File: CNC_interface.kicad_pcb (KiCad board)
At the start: 2 copper layers, 86.4 x 99.1 mm, 35 parts, among them J1 Conn_01x04_Male, J10 Conn_01x08, J11 Conn_01x08, J12 Conn_01x08, J13 Conn_01x08, J14 Conn_01x03_Male, J15 Conn_01x03_Male, J16 Conn_01x03_Male, J17 Conn_01x08, J18 Conn_01x10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

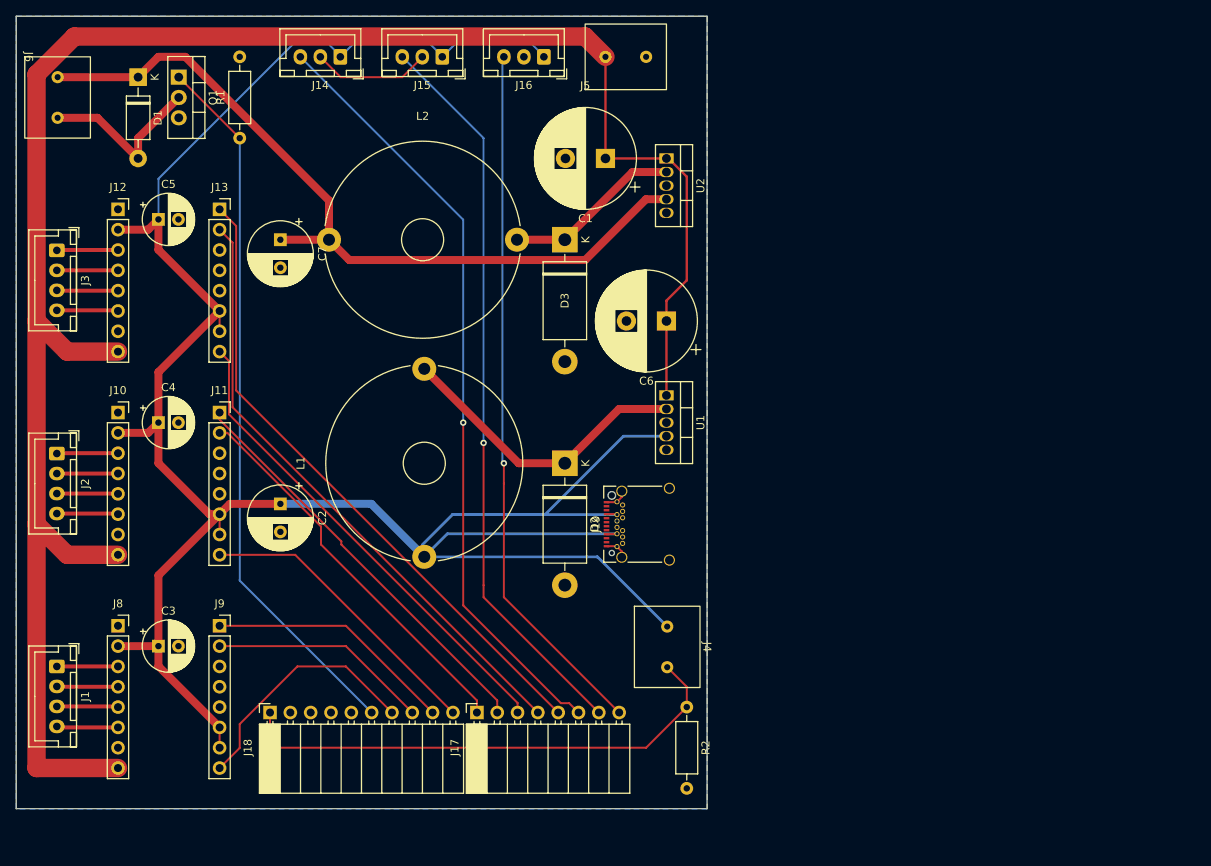
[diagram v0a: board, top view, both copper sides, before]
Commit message: connect step motors to 12V
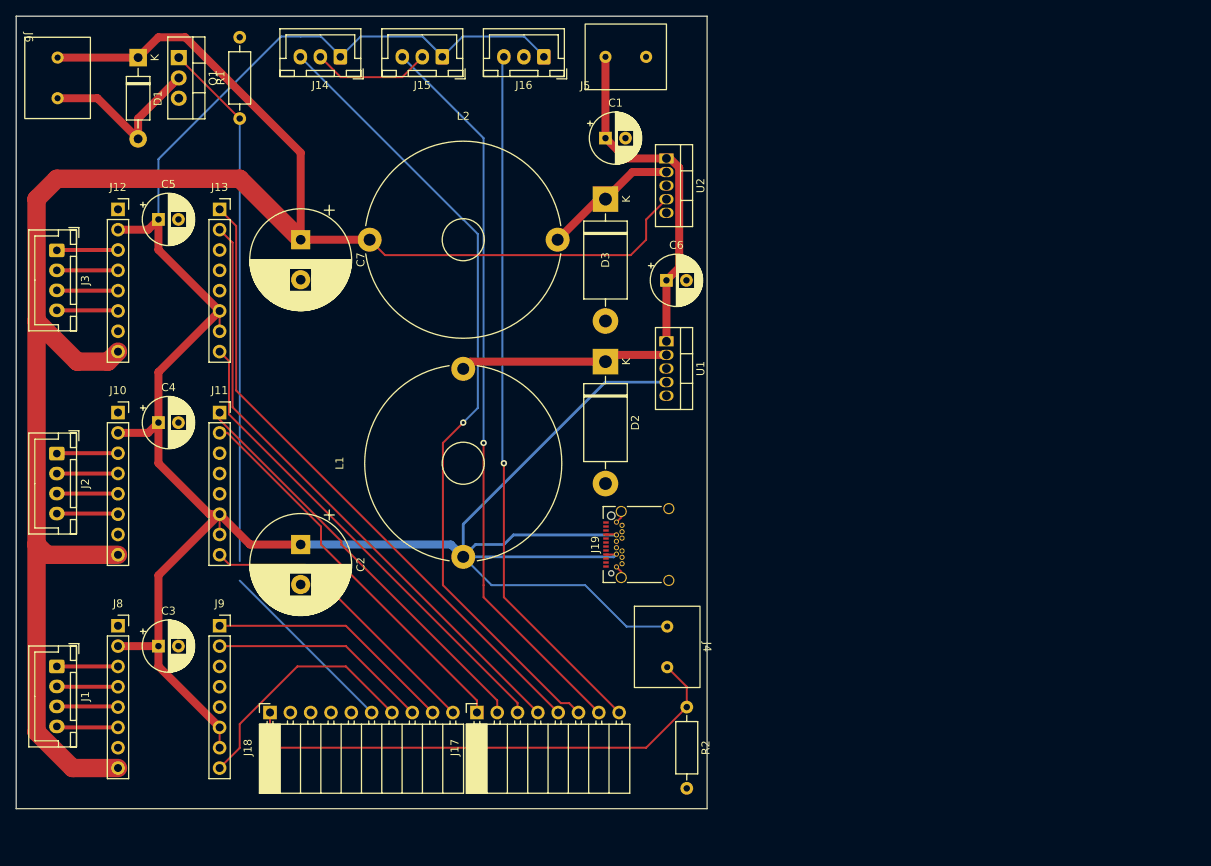
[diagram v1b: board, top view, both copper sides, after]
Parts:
- C1, C6: footprint Capacitor_THT:CP_Radial_D12.5mm_P5.00mm -> Capacitor_THT:CP_Radial_D6.3mm_P2.50mm
- C2, C7: footprint Capacitor_THT:CP_Radial_D8.0mm_P3.50mm -> Capacitor_THT:CP_Radial_D12.5mm_P5.00mm
- moved D2 13.7 mm to (119.4, 73.7)
- moved D3 7.18 mm to (119.4, 53.3)
- moved U1 6.76 mm to (127.0, 71.1)
- moved C2 5.68 mm to (81.3, 96.5)
- moved L2 5.08 mm to (89.9, 58.2)
- moved C6 5.08 mm to (127.0, 63.5), turned to 0 degrees
- moved L1 4.87 mm to (101.4, 98.1)
- moved J19 2.54 mm to (124.5, 96.5)
- moved C7 2.54 mm to (81.3, 58.4)
- moved C1 2.54 mm to (119.4, 45.7), turned to 0 degrees
- moved D1 2.45 mm to (61.0, 35.7)
- moved J6 2.45 mm to (46.8, 33.1)
- moved Q1 2.45 mm to (66.0, 35.7)
- moved R1 2.45 mm to (73.7, 43.3)
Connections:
- J10 pad 8: +24V -> +12V
- J12 pad 8: +24V -> +12V
- J8 pad 8: +24V -> +12V
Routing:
- net +24V: track 246.8 -> 43.5 mm
- net +12V: track 99.8 -> 238.6 mm
- net Net-(D2-Pad1): track 38.0 -> 26.1 mm
- net +5V: track 319.0 -> 312.3 mm
- net Net-(D3-Pad1): track 22.2 -> 17.1 mm
- net Lx: track 97.0 -> 100.6 mm
- net GND: track 20.8 -> 18.1 mm
- removed copper zone on B.Cu, net GND

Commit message: place components
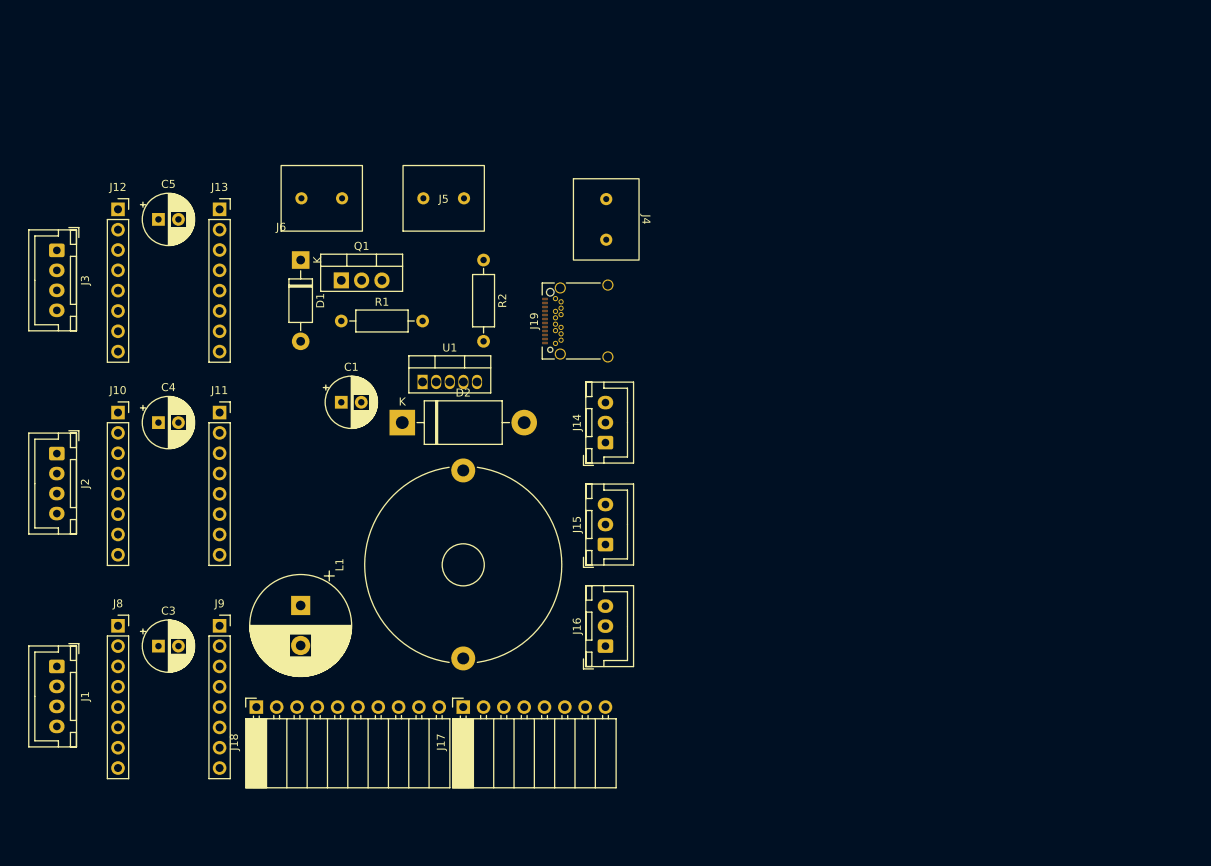
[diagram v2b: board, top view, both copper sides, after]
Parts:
- removed C6: 100µF, Capacitor_THT:CP_Radial_D6.3mm_P2.50mm
- removed C7: 1000µF, Capacitor_THT:CP_Radial_D12.5mm_P5.00mm
- removed D3: 1N5822, Diode_THT:D_DO-201AD_P15.24mm_Horizontal
- removed L2: 220µH, CNC_interface:L_Radial_24.4mm_P23.50mm_Murata_1400series
- removed U2: LM2576HVT-12, Package_TO_SOT_THT:TO-220-5_Vertical
- moved J16 74.1 mm to (119.4, 109.2), turned to 90 degrees
- moved J15 64.3 mm to (119.4, 96.5), turned to 90 degrees
- moved R2 61.4 mm to (104.1, 61.0)
- moved J14 58.5 mm to (119.4, 83.8), turned to 90 degrees
- moved J4 54.0 mm to (115.4, 50.8)
- moved C1 46.7 mm to (86.4, 78.7)
- moved J6 40.2 mm to (78.8, 57.3), turned to 0 degrees
- moved Q1 34.5 mm to (86.4, 63.5), turned to 0 degrees
- moved D1 32.5 mm to (81.3, 61.0)
- moved U1 30.9 mm to (96.5, 76.2), turned to 0 degrees
- moved J19 29.0 mm to (116.8, 68.6)
- moved J5 28.8 mm to (94.1, 57.3)
- moved R1 28.3 mm to (86.4, 68.6), turned to 0 degrees
- moved D2 26.5 mm to (94.0, 81.3), turned to 0 degrees
- moved L1 12.7 mm to (101.4, 110.8)
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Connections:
- C1 pad 1: +24V -> +12V
- J5 pad 1: +24V -> +12V
- U1 pad 1: +24V -> +12V
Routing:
- net +5V: track 312.3 -> 0.00 mm
- net +12V: track 238.6 -> 0.00 mm
- net Lx: track 100.6 -> 0.00 mm, vias 1 -> 0
- net Ly: track 92.1 -> 0.00 mm, vias 1 -> 0
- net DCtrl: track 89.4 -> 0.00 mm
- net Lz: track 88.1 -> 0.00 mm, vias 1 -> 0
- net DIRz: track 80.4 -> 0.00 mm
- net STEPz: track 76.8 -> 0.00 mm
- net CONT: track 63.8 -> 0.00 mm
- net ENz: track 60.5 -> 0.00 mm
- net DIRy: track 51.9 -> 0.00 mm
- net STEPy: track 48.8 -> 0.00 mm
- net +24V: track 43.5 -> 0.00 mm
- net ENy: track 37.3 -> 0.00 mm
- net DIRx: track 31.1 -> 0.00 mm
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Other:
- board outline removed

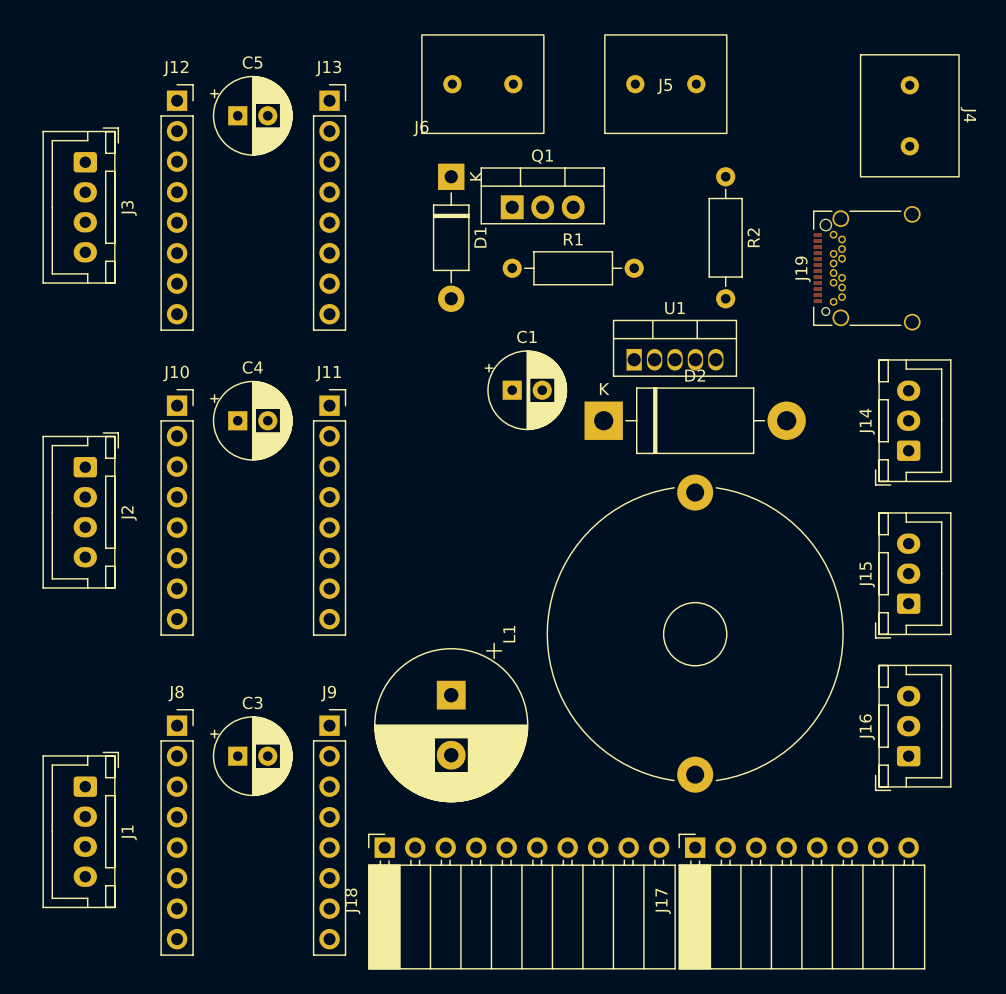
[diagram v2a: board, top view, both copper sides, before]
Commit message: Route PCB + silkscreen
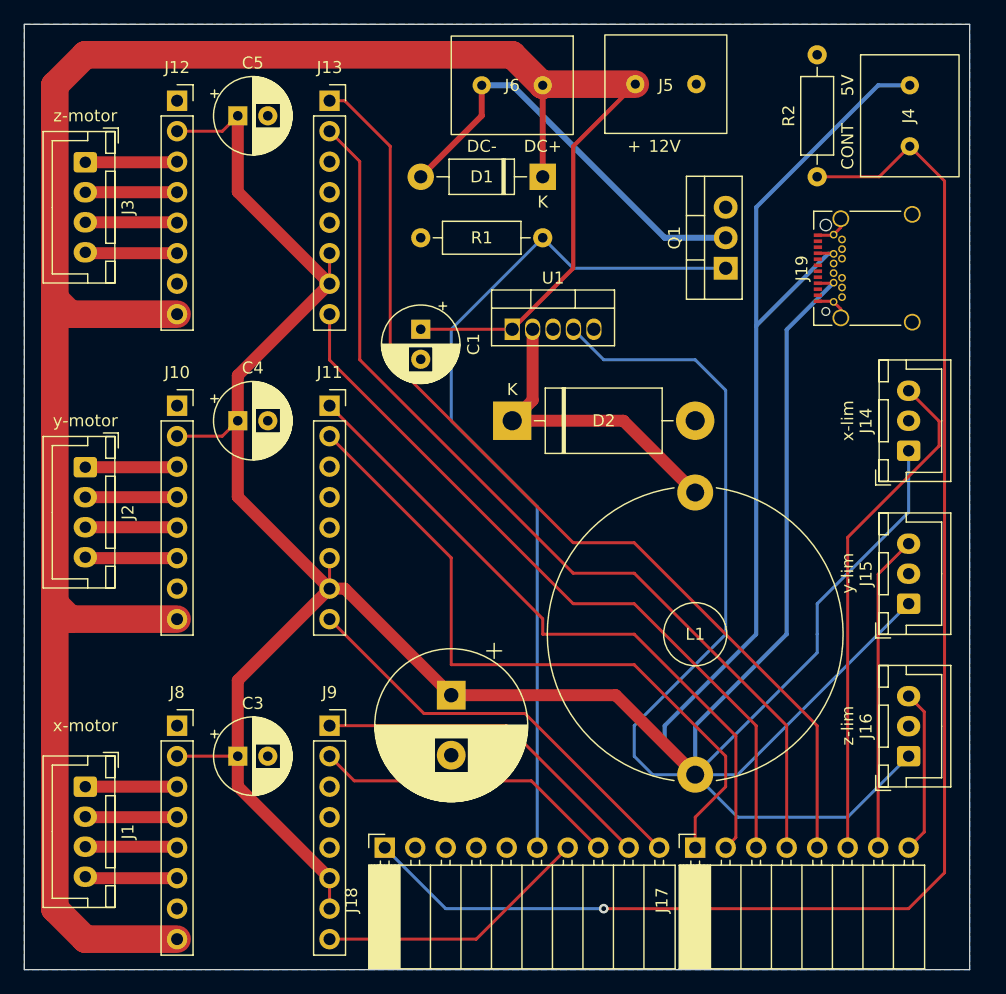
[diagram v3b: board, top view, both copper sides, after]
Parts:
- moved Q1 18.5 mm to (104.1, 68.6), turned to 90 degrees
- moved J6 15.0 mm to (91.4, 49.2), turned to 180 degrees
- moved U1 10.5 mm to (86.4, 73.7)
- moved C1 9.16 mm to (78.7, 73.7), turned to -90 degrees
- moved D1 7.62 mm to (88.9, 61.0), turned to 180 degrees
- moved D2 7.62 mm to (86.4, 81.3)
- moved R2 7.62 mm to (111.8, 61.0), turned to 90 degrees
- moved R1 3.59 mm to (88.9, 66.0), turned to 180 degrees
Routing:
- net +5V: track 0.00 -> 399.7 mm
- net +12V: track 0.00 -> 191.7 mm
- net CONT: track 0.00 -> 120.4 mm, vias 0 -> 1
- net DIRz: track 0.00 -> 82.8 mm
- net STEPz: track 0.00 -> 78.4 mm
- net DCtrl: track 0.00 -> 73.2 mm
- net ENz: track 0.00 -> 62.1 mm
- net STEPy: track 0.00 -> 57.9 mm
- net DIRy: track 0.00 -> 55.6 mm
- net Lx: track 0.00 -> 42.3 mm
- net ENy: track 0.00 -> 35.3 mm
- net DC-: track 0.00 -> 35.3 mm
- net DIRx: track 0.00 -> 29.1 mm
- net Ly: track 0.00 -> 26.4 mm
- net Net-(D2-Pad1): track 0.00 -> 26.0 mm
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- added copper zone on B.Cu, net GND
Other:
- board outline added: 78.7 x 78.7 mm
- board text added: "+"
- board text added: "12V"
- board text added: "5V"
- board text added: "CONT"
- board text added: "DC+"
- board text added: "DC-"
- board text added: "x-lim"
- board text added: "x-motor"
- board text added: "y-lim"
- board text added: "y-motor"
- board text added: "z-lim"
- board text added: "z-motor"

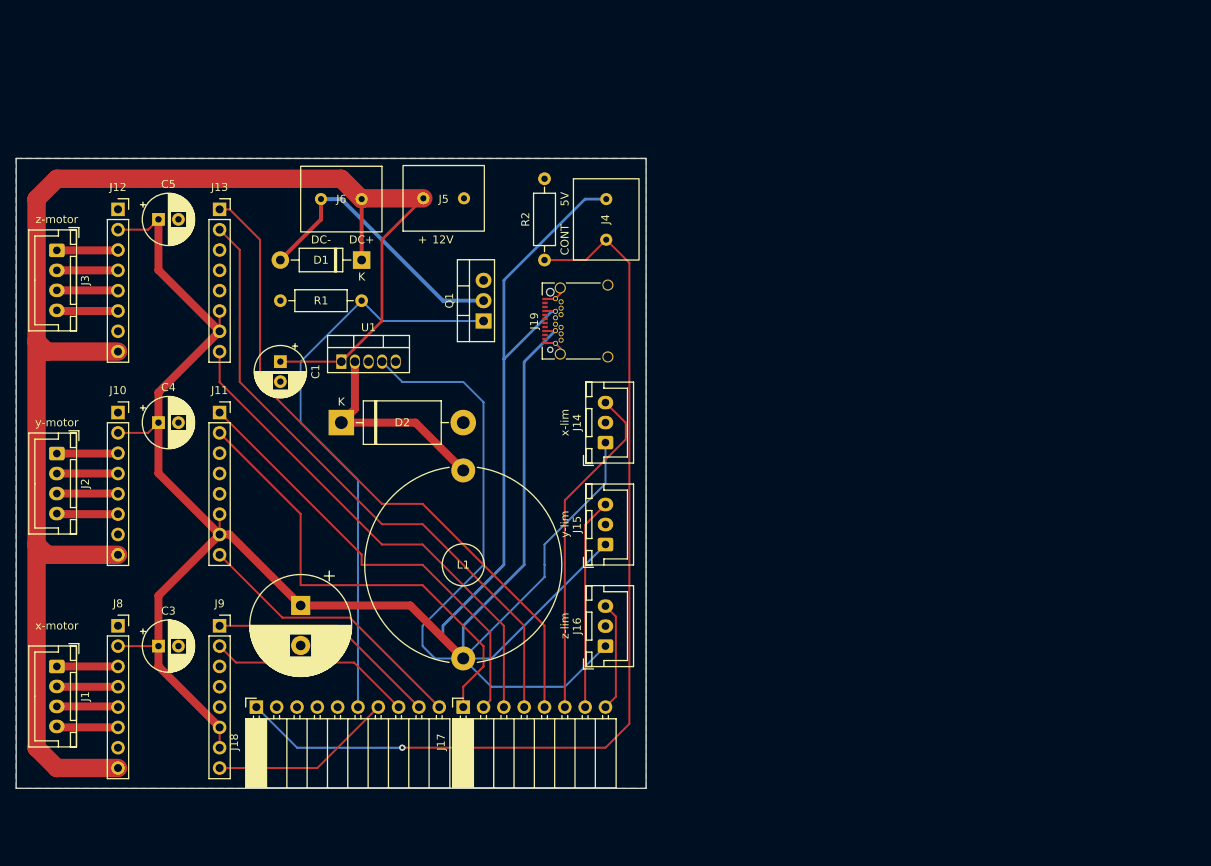
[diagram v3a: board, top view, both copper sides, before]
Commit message: Finish pcb silkscreen and mounting pins
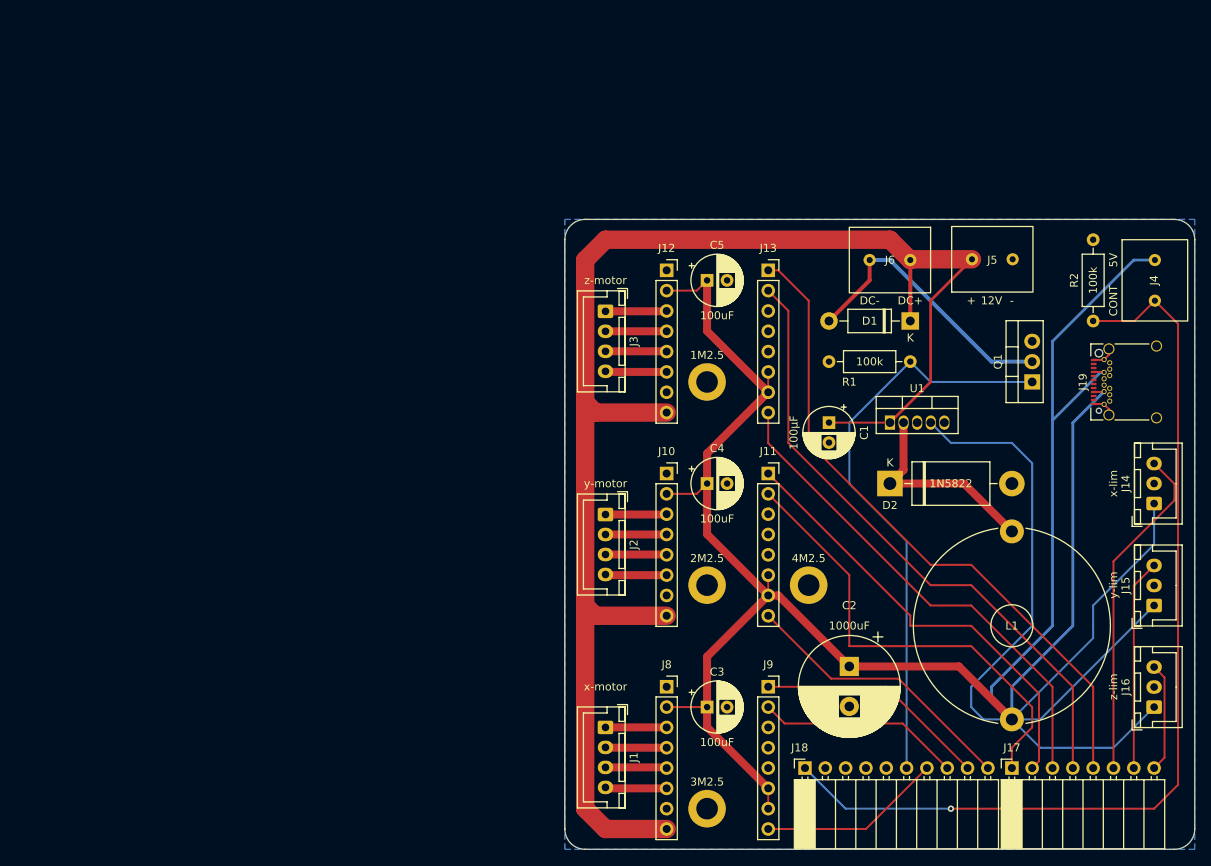
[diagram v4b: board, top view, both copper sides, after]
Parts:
- added 1M2.5: MountingHole_2.7mm_M2.5_DIN965_Pad, MountingHole:MountingHole_2.7mm_M2.5_DIN965_Pad, F.Cu at (132.1, 76.2)
- added 2M2.5: MountingHole_2.7mm_M2.5_DIN965_Pad, MountingHole:MountingHole_2.7mm_M2.5_DIN965_Pad, F.Cu at (132.1, 101.6)
- added 3M2.5: MountingHole_2.7mm_M2.5_DIN965_Pad, MountingHole:MountingHole_2.7mm_M2.5_DIN965_Pad, F.Cu at (132.1, 129.5)
- added 4M2.5: MountingHole_2.7mm_M2.5_DIN965_Pad, MountingHole:MountingHole_2.7mm_M2.5_DIN965_Pad, F.Cu at (144.8, 101.6)
- moved C2 69.0 mm to (149.9, 111.8)
- moved C3 69.0 mm to (132.1, 116.8)
- moved C4 69.0 mm to (132.1, 88.9)
- moved C5 69.0 mm to (132.1, 63.5)
- moved J10 69.0 mm to (127.0, 87.6)
- moved J12 69.0 mm to (127.0, 62.2)
- moved J14 69.0 mm to (188.0, 91.4)
- moved J15 69.0 mm to (188.0, 104.1)
- moved J16 69.0 mm to (188.0, 116.8)
- moved J17 69.0 mm to (170.2, 124.5)
- moved J4 69.0 mm to (184.0, 58.4)
- moved J6 69.0 mm to (160.0, 56.9)
- moved J8 69.0 mm to (127.0, 114.3)
- moved C1 69.0 mm to (147.3, 81.3)
- moved D2 69.0 mm to (154.9, 88.9)
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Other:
- outline, holes or cut-outs redrawn
- board text added: "-"
- board text added: "// ('> /rr *\))_"
- board text added: "Baudin Stanislas"
- board text added: "CNC PCB"
- board text added: "ECAM Projet robotique"
- board text added: "Janssens Victor"
- board text added: "Martinez Sébastien"
- board text added: "Penning Chloé"
- board text added: "TOP"
- board text added: "Vico Nathan"
- board text added: "Yacoub Clément"
